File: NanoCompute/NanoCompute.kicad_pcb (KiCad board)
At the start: 2 copper layers, 62 parts, among them J1 2250506, U1 RTL8211F, U2 MT53E1G32D2FW, U3 HSP051, U4 RK3588, U5 TPS54308, U6 HSP051, U7 TLV74311, U8 TLV74325, Y1 25 MHz

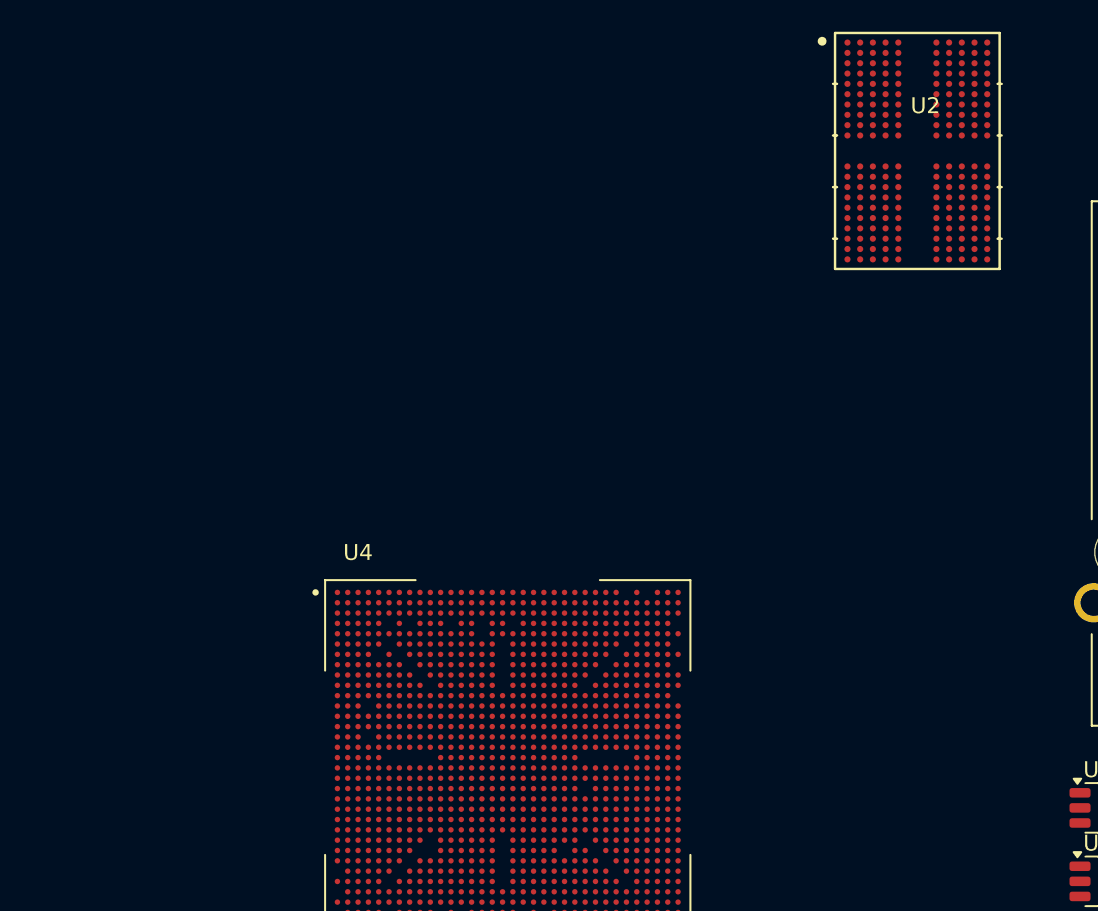
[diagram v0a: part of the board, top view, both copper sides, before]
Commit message: I think I added net classes(+coloring) for LPDDR4.
I'm not sure, it's 3AM I should check what I did tomorrow, figure our
those couple of signals that I don't understand where to connect or what
they are for. Probabbly could start working on the power section of the
LPDDR4. Need to check how much RAM will I actually need for 4K video
(@60fps?).
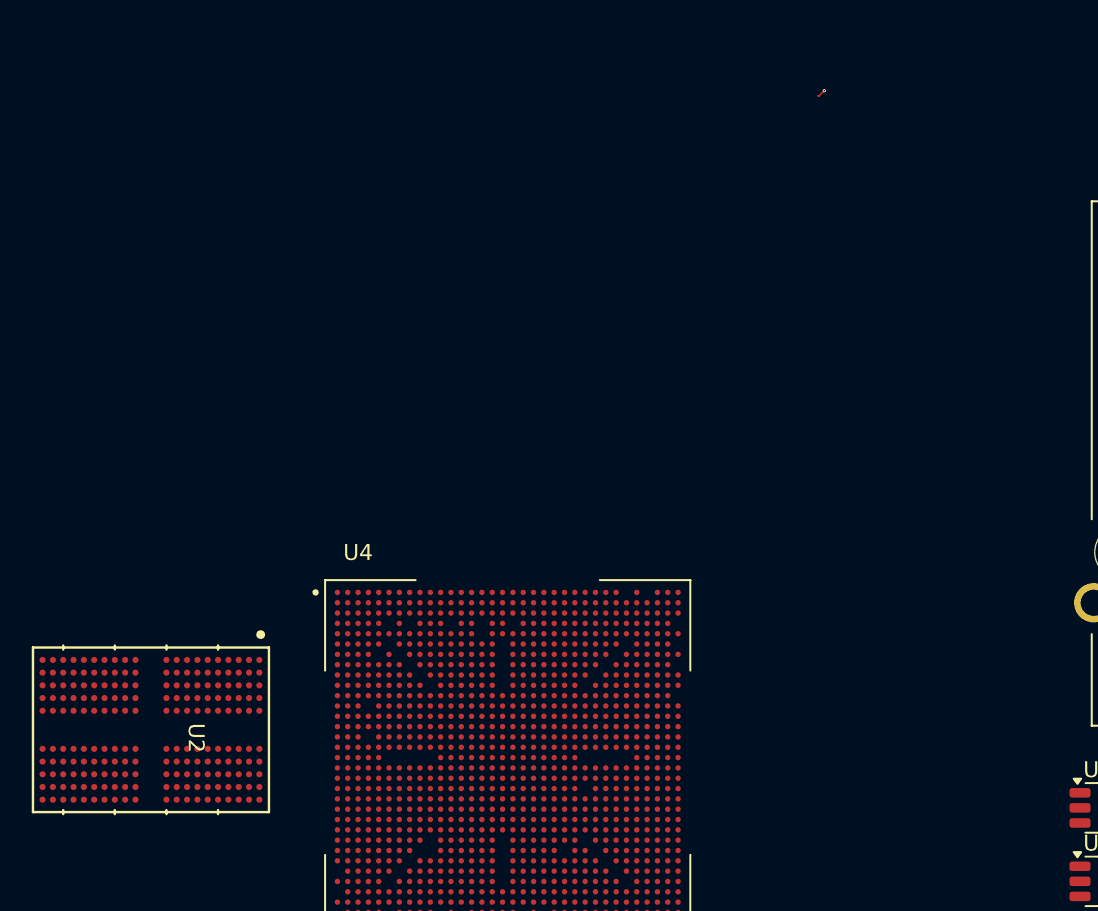
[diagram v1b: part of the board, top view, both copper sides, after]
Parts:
- moved U2 60.5 mm to (94.8, 87.6), turned to -90 degrees
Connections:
- U2 pad A10: unconnected-(U2B-VSS-PadA10) -> GND
- U2 pad A3: unconnected-(U2B-VSS-PadA3) -> GND
- U2 pad AA11: unconnected-(U2A-DQ8_B-PadAA11) -> /LPDDR4/DQ8_B
- U2 pad AA2: unconnected-(U2A-DQ0_B-PadAA2) -> /LPDDR4/DQ0_B
- U2 pad AA4: unconnected-(U2A-DQ7_B-PadAA4) -> /LPDDR4/DQ7_B
- U2 pad AA9: unconnected-(U2A-DQ15_B-PadAA9) -> /LPDDR4/DQ15_B
- U2 pad AB10: unconnected-(U2B-VSS-PadAB10) -> GND
- U2 pad AB3: unconnected-(U2B-VSS-PadAB3) -> GND
- U2 pad AB5: unconnected-(U2B-VSS-PadAB5) -> GND
- U2 pad AB8: unconnected-(U2B-VSS-PadAB8) -> GND
- U2 pad C1: unconnected-(U2B-VSS-PadC1) -> GND
- U2 pad C12: unconnected-(U2B-VSS-PadC12) -> GND
- U2 pad C5: unconnected-(U2B-VSS-PadC5) -> GND
- U2 pad C8: unconnected-(U2B-VSS-PadC8) -> GND
- U2 pad D11: unconnected-(U2B-VSS-PadD11) -> GND
- U2 pad D2: unconnected-(U2B-VSS-PadD2) -> GND
- U2 pad D4: unconnected-(U2B-VSS-PadD4) -> GND
- U2 pad D9: unconnected-(U2B-VSS-PadD9) -> GND
- U2 pad E1: unconnected-(U2B-VSS-PadE1) -> GND
- U2 pad E12: unconnected-(U2B-VSS-PadE12) -> GND
- U2 pad E5: unconnected-(U2B-VSS-PadE5) -> GND
- U2 pad E8: unconnected-(U2B-VSS-PadE8) -> GND
- U2 pad G1: unconnected-(U2B-VSS-PadG1) -> GND
- U2 pad G10: unconnected-(U2B-VSS-PadG10) -> GND
- U2 pad G12: unconnected-(U2B-VSS-PadG12) -> GND
- U2 pad G3: unconnected-(U2B-VSS-PadG3) -> GND
- U2 pad G5: unconnected-(U2B-VSS-PadG5) -> GND
- U2 pad G8: unconnected-(U2B-VSS-PadG8) -> GND
- U2 pad J1: unconnected-(U2B-VSS-PadJ1) -> GND
- U2 pad J10: unconnected-(U2B-VSS-PadJ10) -> GND
- U2 pad J12: unconnected-(U2B-VSS-PadJ12) -> GND
- U2 pad J3: unconnected-(U2B-VSS-PadJ3) -> GND
- U2 pad K11: unconnected-(U2B-VSS-PadK11) -> GND
- U2 pad K2: unconnected-(U2B-VSS-PadK2) -> GND
- U2 pad K4: unconnected-(U2B-VSS-PadK4) -> GND
- U2 pad K9: unconnected-(U2B-VSS-PadK9) -> GND
- U2 pad N11: unconnected-(U2B-VSS-PadN11) -> GND
- U2 pad N2: unconnected-(U2B-VSS-PadN2) -> GND
- U2 pad N4: unconnected-(U2B-VSS-PadN4) -> GND
- U2 pad N9: unconnected-(U2B-VSS-PadN9) -> GND
- U2 pad P1: unconnected-(U2B-VSS-PadP1) -> GND
- U2 pad P10: unconnected-(U2B-VSS-PadP10) -> GND
- U2 pad P12: unconnected-(U2B-VSS-PadP12) -> GND
- U2 pad P3: unconnected-(U2B-VSS-PadP3) -> GND
- U2 pad T1: unconnected-(U2B-VSS-PadT1) -> GND
- U2 pad T10: unconnected-(U2B-VSS-PadT10) -> GND
- U2 pad T12: unconnected-(U2B-VSS-PadT12) -> GND
- U2 pad T3: unconnected-(U2B-VSS-PadT3) -> GND
- U2 pad T5: unconnected-(U2B-VSS-PadT5) -> GND
- U2 pad T8: unconnected-(U2B-VSS-PadT8) -> GND
- U2 pad U11: unconnected-(U2A-DQ11_B-PadU11) -> /LPDDR4/DQ11_B
- U2 pad U2: unconnected-(U2A-DQ3_B-PadU2) -> /LPDDR4/DQ3_B
- U2 pad U4: unconnected-(U2A-DQ4_B-PadU4) -> /LPDDR4/DQ4_B
- U2 pad U9: unconnected-(U2A-DQ12_B-PadU9) -> /LPDDR4/DQ12_B
- U2 pad V1: unconnected-(U2B-VSS-PadV1) -> GND
- U2 pad V11: unconnected-(U2A-DQ10_B-PadV11) -> /LPDDR4/DQ10_B
- U2 pad V12: unconnected-(U2B-VSS-PadV12) -> GND
- U2 pad V2: unconnected-(U2A-DQ2_B-PadV2) -> /LPDDR4/DQ2_B
- U2 pad V4: unconnected-(U2A-DQ5_B-PadV4) -> /LPDDR4/DQ5_B
- U2 pad V5: unconnected-(U2B-VSS-PadV5) -> GND
- U2 pad V8: unconnected-(U2B-VSS-PadV8) -> GND
- U2 pad V9: unconnected-(U2A-DQ13_B-PadV9) -> /LPDDR4/DQ13_B
- U2 pad W11: unconnected-(U2B-VSS-PadW11) -> GND
- U2 pad W2: unconnected-(U2B-VSS-PadW2) -> GND
- U2 pad W4: unconnected-(U2B-VSS-PadW4) -> GND
- U2 pad W9: unconnected-(U2B-VSS-PadW9) -> GND
- U2 pad Y1: unconnected-(U2B-VSS-PadY1) -> GND
- U2 pad Y11: unconnected-(U2A-DQ9_B-PadY11) -> /LPDDR4/DQ9_B
- U2 pad Y12: unconnected-(U2B-VSS-PadY12) -> GND
- U2 pad Y2: unconnected-(U2A-DQ1_B-PadY2) -> /LPDDR4/DQ1_B
- U2 pad Y4: unconnected-(U2A-DQ6_B-PadY4) -> /LPDDR4/DQ6_B
- U2 pad Y5: unconnected-(U2B-VSS-PadY5) -> GND
- U2 pad Y8: unconnected-(U2B-VSS-PadY8) -> GND
- U2 pad Y9: unconnected-(U2A-DQ14_B-PadY9) -> /LPDDR4/DQ14_B
- U4 pad AA1: unconnected-(U4A-DDR_CH0_DQ14_A-PadAA1) -> /LPDDR4/DQ14_A
- U4 pad AA2: unconnected-(U4A-DDR_CH0_DQ15_A-PadAA2) -> /LPDDR4/DQ15_A
- U4 pad AB1: unconnected-(U4A-DDR_CH0_DQ9_A-PadAB1) -> /LPDDR4/DQ9_A
- U4 pad AB2: unconnected-(U4A-DDR_CH0_DQ8_A-PadAB2) -> /LPDDR4/DQ8_A
- U4 pad AC1: unconnected-(U4A-DDR_CH0_DQ10_A-PadAC1) -> /LPDDR4/DQ10_A
- U4 pad AC2: unconnected-(U4A-DDR_CH0_DQ11_A-PadAC2) -> /LPDDR4/DQ11_A
- U4 pad R2: unconnected-(U4A-DDR_CH0_DQ3_A-PadR2) -> /LPDDR4/DQ3_A
- U4 pad T1: unconnected-(U4A-DDR_CH0_DQ2_A-PadT1) -> /LPDDR4/DQ2_A
- U4 pad T2: unconnected-(U4A-DDR_CH0_DQ1_A-PadT2) -> /LPDDR4/DQ1_A
- U4 pad U1: unconnected-(U4A-DDR_CH0_DQ0_A-PadU1) -> /LPDDR4/DQ0_A
- U4 pad U2: unconnected-(U4A-DDR_CH0_DQ7_A-PadU2) -> /LPDDR4/DQ7_A
- U4 pad V1: unconnected-(U4A-DDR_CH0_DQ6_A-PadV1) -> /LPDDR4/DQ6_A
- U4 pad V2: unconnected-(U4A-DDR_CH0_DQ5_A-PadV2) -> /LPDDR4/DQ5_A
- U4 pad W1: unconnected-(U4A-DDR_CH0_DQ4_A-PadW1) -> /LPDDR4/DQ4_A
- U4 pad Y1: unconnected-(U4A-DDR_CH0_DQ12_A-PadY1) -> /LPDDR4/DQ12_A
- U4 pad Y2: unconnected-(U4A-DDR_CH0_DQ13_A-PadY2) -> /LPDDR4/DQ13_A
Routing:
- net /LPDDR4/DQ6_A: track 0.00 -> 0.54 mm, vias 0 -> 1

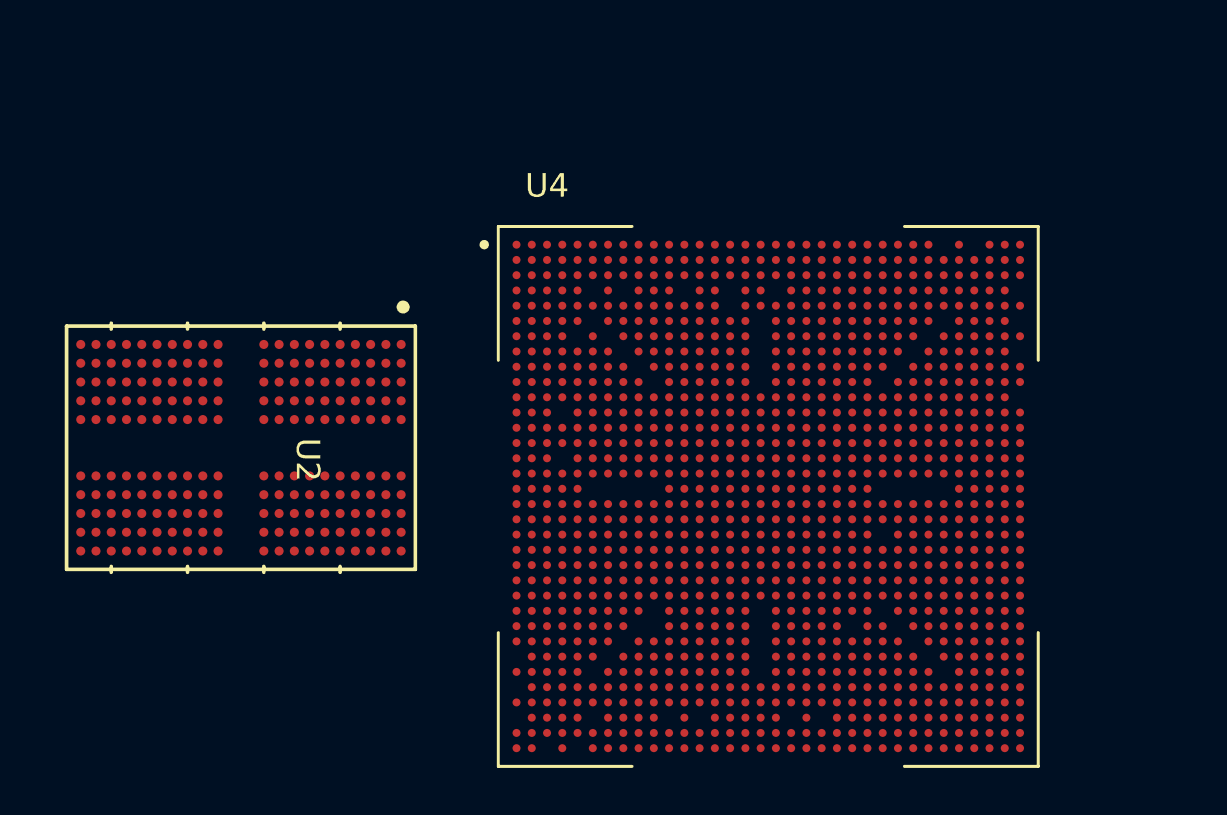
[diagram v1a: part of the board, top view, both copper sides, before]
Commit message: Finished one LPDDR4 and connected it to LPDDR4 PHY
Connected the LPDDR4 to RK3588 LPDDR4 PHY, check all connections and it LGTM!
Added a second chip for additional 32Gb(4GB) LPDDR4 for total of 64Gb(8GB) of LPDRR4 memory.
Need to change nets for second chip from A->C and B->D.
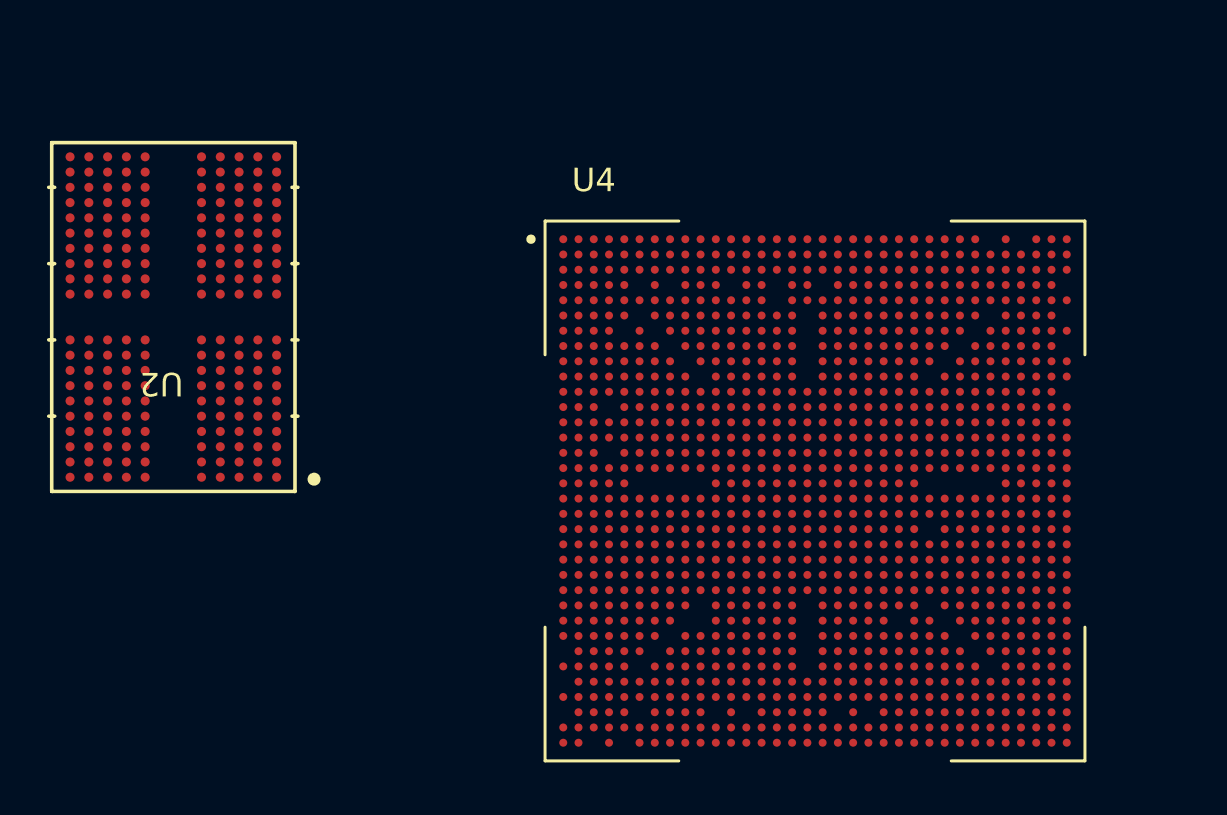
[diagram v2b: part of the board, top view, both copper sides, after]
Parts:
- moved U2 6.27 mm to (91.9, 82.1), turned to 180 degrees
- moved U4 2.00 mm to (119.2, 89.5)
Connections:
- U2 pad C10: unconnected-(U2A-DMI1_A-PadC10) -> /LPDDR4/DMI1_A
- U2 pad C3: unconnected-(U2A-DMI0_A-PadC3) -> /LPDDR4/DMIO_A
- U2 pad H10: unconnected-(U2A-CA3_A-PadH10) -> /LPDDR4/CA3_A
- U2 pad H11: unconnected-(U2A-CA4_A-PadH11) -> /LPDDR4/CA4_A
- U2 pad H2: unconnected-(U2A-CA0_A-PadH2) -> /LPDDR4/CA0_A
- U2 pad H3: unconnected-(U2A-CS1_A-PadH3) -> /LPDDR4/CS1_A
- U2 pad H4: unconnected-(U2A-CS0_A-PadH4) -> /LPDDR4/CS0_A
- U2 pad H9: unconnected-(U2A-CA2_A-PadH9) -> /LPDDR4/CA2_A
- U2 pad J11: unconnected-(U2A-CA5_A-PadJ11) -> /LPDDR4/CA5_A
- U2 pad J2: unconnected-(U2A-CA1_A-PadJ2) -> /LPDDR4/CA1_A
- U2 pad J4: unconnected-(U2A-CKE0_A-PadJ4) -> /LPDDR4/CKE0_A
- U2 pad J5: unconnected-(U2A-CKE1_A-PadJ5) -> /LPDDR4/CKE1_A
- U2 pad J8: unconnected-(U2A-CK_t_A-PadJ8) -> /LPDDR4/CK_A_P
- U2 pad J9: unconnected-(U2A-CK_c_A-PadJ9) -> /LPDDR4/CK_A_N
- U2 pad P11: unconnected-(U2A-CA5_B-PadP11) -> /LPDDR4/CA5_A
- U2 pad P2: unconnected-(U2A-CA1_B-PadP2) -> /LPDDR4/CA1_A
- U2 pad P4: unconnected-(U2A-CKE0_B-PadP4) -> /LPDDR4/CKE0_A
- U2 pad P5: unconnected-(U2A-CKE1_B-PadP5) -> /LPDDR4/CKE1_A
- U2 pad P8: unconnected-(U2A-CK_t_B-PadP8) -> /LPDDR4/CK_A_P
- U2 pad P9: unconnected-(U2A-CK_c_B-PadP9) -> /LPDDR4/CK_A_N
- U2 pad R10: unconnected-(U2A-CA3_B-PadR10) -> /LPDDR4/CA3_A
- U2 pad R11: unconnected-(U2A-CA4_B-PadR11) -> /LPDDR4/CA4_A
- U2 pad R2: unconnected-(U2A-CA0_B-PadR2) -> /LPDDR4/CA0_A
- U2 pad R3: unconnected-(U2A-CS1_B-PadR3) -> /LPDDR4/CS0_A
- U2 pad R4: unconnected-(U2A-CS0_B-PadR4) -> /LPDDR4/CS1_A
- U2 pad R9: unconnected-(U2A-CA2_B-PadR9) -> /LPDDR4/CA2_A
- U2 pad Y10: unconnected-(U2A-DMI1_B-PadY10) -> /LPDDR4/DMI1_A
- U2 pad Y3: unconnected-(U2A-DMI0_B-PadY3) -> /LPDDR4/DMIO_A
- U4 pad B1: unconnected-(U4A-DDR_CH0_DQ11_B-PadB1) -> /LPDDR4/DQ11_B
- U4 pad C1: unconnected-(U4A-DDR_CH0_DQ9_B-PadC1) -> /LPDDR4/DQ9_B
- U4 pad C2: unconnected-(U4A-DDR_CH0_DQ10_B-PadC2) -> /LPDDR4/DQ10_B
- U4 pad D1: unconnected-(U4A-DDR_CH0_DQ15_B-PadD1) -> /LPDDR4/DQ15_B
- U4 pad D2: unconnected-(U4A-DDR_CH0_DQ8_B-PadD2) -> /LPDDR4/DQ8_B
- U4 pad E1: unconnected-(U4A-DDR_CH0_DQ13_B-PadE1) -> /LPDDR4/DQ13_B
- U4 pad E2: unconnected-(U4A-DDR_CH0_DQ14_B-PadE2) -> /LPDDR4/DQ14_B
- U4 pad F1: unconnected-(U4A-DDR_CH0_DQ4_B-PadF1) -> /LPDDR4/DQ4_B
- U4 pad F2: unconnected-(U4A-DDR_CH0_DQ12_B-PadF2) -> /LPDDR4/DQ12_B
- U4 pad G1: unconnected-(U4A-DDR_CH0_DQ6_B-PadG1) -> /LPDDR4/DQ6_B
- U4 pad G2: unconnected-(U4A-DDR_CH0_DQ5_B-PadG2) -> /LPDDR4/DQ5_B
- U4 pad H1: unconnected-(U4A-DDR_CH0_DQ0_B-PadH1) -> /LPDDR4/DQ0_B
- U4 pad H2: unconnected-(U4A-DDR_CH0_DQ7_B-PadH2) -> /LPDDR4/DQ7_B
- U4 pad J1: unconnected-(U4A-DDR_CH0_DQ2_B-PadJ1) -> /LPDDR4/DQ2_B
- U4 pad J2: unconnected-(U4A-DDR_CH0_DQ1_B-PadJ2) -> /LPDDR4/DQ1_B
- U4 pad K2: unconnected-(U4A-DDR_CH0_DQ3_B-PadK2) -> /LPDDR4/DQ3_B
- U4 pad N7: unconnected-(U4A-DDR_CH0_LP4/4X_CKE1/LP5_CS1_A-PadN7) -> /LPDDR4/CKE1_A
- U4 pad P2: unconnected-(U4A-DDR_CH0_A5_A-PadP2) -> /LPDDR4/CA5_A
- U4 pad P4: unconnected-(U4A-DDR_CH0_A2_A-PadP4) -> /LPDDR4/CA2_A
- U4 pad P5: unconnected-(U4A-DDR_CH0_A3_A-PadP5) -> /LPDDR4/CA3_A
- U4 pad P7: unconnected-(U4A-DDR_CH0_LP4/4X_CKE0/LP5_CS0_A-PadP7) -> /LPDDR4/CKE0_A
- U4 pad R1: unconnected-(U4A-DDR_CH0_A4_A-PadR1) -> /LPDDR4/CA4_A
- U4 pad R6: unconnected-(U4A-DDR_CH0_LP4/4X_CS0_A-PadR6) -> /LPDDR4/CS0_A
- U4 pad R7: unconnected-(U4A-DDR_CH0_LP4/4X_CS1_A-PadR7) -> /LPDDR4/CS1_A
- U4 pad T7: unconnected-(U4A-DDR_CH0_A0_A-PadT7) -> /LPDDR4/CA0_A
- U4 pad T8: unconnected-(U4A-DDR_CH0_A1_A-PadT8) -> /LPDDR4/CA1_A
